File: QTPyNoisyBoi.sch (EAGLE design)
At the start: 32 parts, among them IC1 LD117AS50TR, IC2 TL074D, J1 WQP-PJ301M-12_JACK, J2 WQP-PJ301M-12_JACK, J3 WQP-PJ301M-12_JACK, J4 WQP-PJ301M-12_JACK, U1 ADAFRUIT_QTPYM0

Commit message: added cap on vmidref; various cleanup
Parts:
- added C9: (no value), rcl:C-EUC0603
- added R14: (no value), rcl:R-EU_R0603
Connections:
- new net N$5: J4.2, R14.2
- net GND: now also C9.1
- net RX: now also R14.1, U1.RX; no longer J4.2
- net VMIDREF: now also C9.2
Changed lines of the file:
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@@
 <part name="D2" library="SparkFun-DiscreteSemi" library_urn="urn:adsk.eagle:library:514" deviceset="DIODE-SCHOTTKY" device="-PMEG4005EJ" package3d_urn="urn:adsk.eagle:package:38441/1" value="0.5A/40V/420mV"/>
 <part name="D1" library="SparkFun-DiscreteSemi" library_urn="urn:adsk.eagle:library:514" deviceset="DIODE-SCHOTTKY" device="-PMEG4005EJ" package3d_urn="urn:adsk.eagle:package:38441/1" value="0.5A/40V/420mV"/>
+<part name="C9" library="rcl" library_urn="urn:adsk.eagle:library:334" deviceset="C-EU" device="C0603" package3d_urn="urn:adsk.eagle:package:23616/2"/>
+<part name="R14" library="rcl" library_urn="urn:adsk.eagle:library:334" deviceset="R-EU_" device="R0603" package3d_urn="urn:adsk.eagle:package:23555/3"/>
 </parts>
 <sheets>
@@
 <attribute name="VALUE" x="192.532" y="104.14" size="1.778" layer="96" font="vector" rot="R90" align="top-left"/>
 </instance>
+<instance part="C9" gate="G$1" x="63.5" y="5.08" smashed="yes" rot="R180">
+<attribute name="NAME" x="61.976" y="4.699" size="1.778" layer="95" rot="R180"/>
+<attribute name="VALUE" x="61.976" y="9.779" size="1.778" layer="96" rot="R180"/>
+</instance>
+<instance part="R14" gate="G$1" x="198.12" y="101.6" smashed="yes">
+<attribute name="NAME" x="194.31" y="103.0986" size="1.778" layer="95"/>
+<attribute name="VALUE" x="194.31" y="98.298" size="1.778" layer="96"/>
+</instance>
 </instances>
 <busses>
@@
 <pinref part="R11" gate="G$1" pin="1"/>
 <pinref part="GND14" gate="1" pin="GND"/>
+<pinref part="C9" gate="G$1" pin="1"/>
+<wire x1="63.5" y1="2.54" x2="71.12" y2="2.54" width="0.1524" layer="91"/>
+<junction x="71.12" y="2.54"/>
 </segment>
 <segment>
@@
 <junction x="71.12" y="12.7"/>
 <label x="76.2" y="12.7" size="1.778" layer="95"/>
+<wire x1="71.12" y1="12.7" x2="63.5" y2="12.7" width="0.1524" layer="91"/>
+<pinref part="C9" gate="G$1" pin="2"/>
+<wire x1="63.5" y1="12.7" x2="63.5" y2="10.16" width="0.1524" layer="91"/>
 </segment>
 <segment>
@@
 <net name="RX" class="0">
 <segment>
-<pinref part="J4" gate="G$1" pin="2"/>
-<wire x1="208.28" y1="101.6" x2="190.5" y2="101.6" width="0.1524" layer="91"/>
 <pinref part="D1" gate="G$1" pin="A"/>
+<pinref part="D2" gate="G$1" pin="C"/>
 <wire x1="190.5" y1="104.14" x2="190.5" y2="101.6" width="0.1524" layer="91"/>
-<pinref part="D2" gate="G$1" pin="C"/>
+<pinref part="R14" gate="G$1" pin="1"/>
 <wire x1="190.5" y1="101.6" x2="190.5" y2="99.06" width="0.1524" layer="91"/>
+<wire x1="193.04" y1="101.6" x2="190.5" y2="101.6" width="0.1524" layer="91"/>
 <junction x="190.5" y="101.6"/>
 <wire x1="190.5" y1="101.6" x2="175.26" y2="101.6" width="0.1524" layer="91"/>
 <label x="175.26" y="101.6" size="1.778" layer="95"/>
 </segment>
-</net>
+<segment>
+<pinref part="U1" gate="U$1" pin="RX"/>
+<wire x1="78.74" y1="45.72" x2="91.44" y2="45.72" width="0.1524" layer="91"/>
+<label x="83.82" y="45.72" size="1.778" layer="95"/>
+</segment>
+</net>
+<net name="N$5" class="0">
+<segment>
+<pinref part="R14" gate="G$1" pin="2"/>
+<pinref part="J4" gate="G$1" pin="2"/>
+<wire x1="203.2" y1="101.6" x2="208.28" y2="101.6" width="0.1524" layer="91"/>
+</segment>
+</net>

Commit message: sigh
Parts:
- added C10: 18pF, rcl:C-EUC0603
- added C11: (no value), rcl:C-EUC0603
- added D3, D4: 250mA/100V, halcyonmod_DiscreteSemi:DIODEBAS16
- added S1: MOMENTARY-SWITCH-SPST-PTH-6.0MM, SparkFun-Switches:MOMENTARY-SWITCH-SPST-PTH-6.0MM
- C4: value (none) -> 0.1uF
- R10, R11: value (none) -> 47k
- R4: value (none) -> 33k
- R5: value (none) -> 100k
- R6: value (none) -> 200
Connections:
- net N$2 renamed A1
- net N$3 renamed A2
- net N$4 renamed A3
- net VMIDREF renamed VBIAS
- removed net N$15: J2.2, R9.2
- new net N$12: D4.C, DIM1.-12V
- new net N$17: D3.A, DIM1.+12V
- new net N$18: C10.2, IC2A.OUT, R6.1
- new net N$2: S1.2, U1.TX
- new net N$8: IC2D.-IN, IC2D.OUT
- net +12V: now also D3.C; no longer DIM1.+12V
- net -12V: now also D4.A; no longer DIM1.-12V
- net GND: now also IC2D.+IN, S1.1
- net N$1: now also J2.2, R9.2; no longer IC2B.OUT, R9.1
- net N$10: now also C10.1
- net N$13: now also C11.1
- net N$14: now also C11.2, IC2B.OUT, R9.1; no longer J1.2, R6.2
- net N$9: now also J1.2, R6.2; no longer IC2A.OUT, R6.1
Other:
- moved on the sheet: C4, C5, C6, C7, D1, D2, J4, R14, R5, R6, R8, R9

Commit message: submit to fab
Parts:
- added C12: 18pF, rcl:C-EUC0603
- added R144: 220, rcl:R-EU_R0603
- C1, C2: value (none) -> 1uF
- C11: value (none) -> 18pF
- C3, C5, C6, C7, C8, C9: value (none) -> 0.1uF
- R1, R2, R3: value (none) -> 10k
- R10, R11: value 47k -> 33k
- R12, R7: value (none) -> 33k
- R13, R8: value (none) -> 100k
- R14, R9: value (none) -> 200
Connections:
- removed net N$16: J3.2, R13.2
- new net N$3: C12.2, IC2C.OUT, R14.1
- new net N$4: C12.1, C8.1, IC2C.+IN, R12.2, R13.1
- net A0: no longer C8.1, IC2C.+IN
- net N$11: now also J3.2, R13.2, R14.2; no longer IC2C.OUT, R12.2, R13.1
- net N$5: now also R144.2; no longer R14.2
- net RX: now also R144.1; no longer R14.1
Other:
- moved on the sheet: C1, C10, C11, C2, C3, C4, C5, C8, D1, D2, D3, D4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

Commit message: fix dumb +/- opamp input swap on B and C
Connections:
- net N$13: now also IC2B.-IN; no longer IC2B.+IN
- net N$4: now also IC2C.-IN; no longer IC2C.+IN
- net VBIAS: now also IC2B.+IN, IC2C.+IN; no longer IC2B.-IN, IC2C.-IN
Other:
- moved on the sheet: IC2B, IC2C
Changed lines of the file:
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@@
 <part name="C12" library="rcl" library_urn="urn:adsk.eagle:library:334" deviceset="C-EU" device="C0603" package3d_urn="urn:adsk.eagle:package:23616/2" value="18pF"/>
 <part name="R12" library="rcl" library_urn="urn:adsk.eagle:library:334" deviceset="R-EU_" device="R0603" package3d_urn="urn:adsk.eagle:package:23555/3" value="33k"/>
-<part name="FRAME1" library="frames" library_urn="urn:adsk.eagle:library:229" deviceset="A3L-LOC" device=""/>
+<part name="FRAME1" library="frames" library_urn="urn:adsk.eagle:library:229" deviceset="A3L-LOC" device="" value="QTPyNoisyBoi"/>
 </parts>
 <sheets>
@@
 <attribute name="VALUE" x="139.7" y="71.12" size="1.778" layer="96" rot="MR180"/>
 </instance>
-<instance part="IC2" gate="B" x="139.7" y="20.32" smashed="yes">
-<attribute name="NAME" x="142.24" y="23.495" size="1.778" layer="95"/>
-<attribute name="VALUE" x="141.224" y="14.732" size="1.778" layer="96"/>
-</instance>
-<instance part="IC2" gate="C" x="139.7" y="-27.94" smashed="yes">
-<attribute name="NAME" x="142.24" y="-24.765" size="1.778" layer="95"/>
-<attribute name="VALUE" x="142.24" y="-33.02" size="1.778" layer="96"/>
+<instance part="IC2" gate="B" x="139.7" y="20.32" smashed="yes" rot="MR180">
+<attribute name="NAME" x="142.24" y="17.145" size="1.778" layer="95" rot="MR180"/>
+<attribute name="VALUE" x="141.224" y="25.908" size="1.778" layer="96" rot="MR180"/>
+</instance>
+<instance part="IC2" gate="C" x="139.7" y="-27.94" smashed="yes" rot="MR180">
+<attribute name="NAME" x="142.24" y="-31.115" size="1.778" layer="95" rot="MR180"/>
+<attribute name="VALUE" x="142.24" y="-22.86" size="1.778" layer="96" rot="MR180"/>
 </instance>
 <instance part="IC2" gate="D" x="139.7" y="-60.96" smashed="yes">
@@
 <pinref part="R7" gate="G$1" pin="2"/>
 <wire x1="127" y1="22.86" x2="129.54" y2="22.86" width="0.1524" layer="91"/>
-<pinref part="IC2" gate="B" pin="+IN"/>
-<wire x1="132.08" y1="22.86" x2="129.54" y2="22.86" width="0.1524" layer="91"/>
-<junction x="129.54" y="22.86"/>
 <pinref part="C11" gate="G$1" pin="1"/>
 <wire x1="129.54" y1="33.02" x2="134.62" y2="33.02" width="0.1524" layer="91"/>
 <junction x="129.54" y="33.02"/>
+<pinref part="IC2" gate="B" pin="-IN"/>
+<wire x1="129.54" y1="22.86" x2="132.08" y2="22.86" width="0.1524" layer="91"/>
+<junction x="129.54" y="22.86"/>
 </segment>
 </net>
@@
 </segment>
 <segment>
-<pinref part="IC2" gate="B" pin="-IN"/>
+<pinref part="IC2" gate="B" pin="+IN"/>
 <wire x1="132.08" y1="17.78" x2="119.38" y2="17.78" width="0.1524" layer="91"/>
 <label x="119.38" y="17.78" size="1.778" layer="95"/>
 </segment>
 <segment>
-<pinref part="IC2" gate="C" pin="-IN"/>
+<pinref part="IC2" gate="C" pin="+IN"/>
 <wire x1="132.08" y1="-30.48" x2="119.38" y2="-30.48" width="0.1524" layer="91"/>
-<label x="119.38" y="-30.48" size="1.778" layer="95"/>
 </segment>
 </net>
@@
 <net name="N$4" class="0">
 <segment>
-<pinref part="IC2" gate="C" pin="+IN"/>
 <pinref part="R12" gate="G$1" pin="2"/>
-<wire x1="132.08" y1="-25.4" x2="129.54" y2="-25.4" width="0.1524" layer="91"/>
 <pinref part="C12" gate="G$1" pin="1"/>
 <wire x1="129.54" y1="-25.4" x2="127" y2="-25.4" width="0.1524" layer="91"/>
 <wire x1="134.62" y1="-17.78" x2="129.54" y2="-17.78" width="0.1524" layer="91"/>
 <wire x1="129.54" y1="-17.78" x2="129.54" y2="-25.4" width="0.1524" layer="91"/>
-<junction x="129.54" y="-25.4"/>
 <pinref part="R13" gate="G$1" pin="1"/>
 <wire x1="134.62" y1="-10.16" x2="129.54" y2="-10.16" width="0.1524" layer="91"/>
@@
 <wire x1="129.54" y1="-2.54" x2="129.54" y2="-10.16" width="0.1524" layer="91"/>
 <junction x="129.54" y="-10.16"/>
+<pinref part="IC2" gate="C" pin="-IN"/>
+<wire x1="129.54" y1="-25.4" x2="132.08" y2="-25.4" width="0.1524" layer="91"/>
+<junction x="129.54" y="-25.4"/>
 </segment>
 </net>
@@
 </sheet>
 </sheets>
+<errors>
+</errors>
 </schematic>
 </drawing>

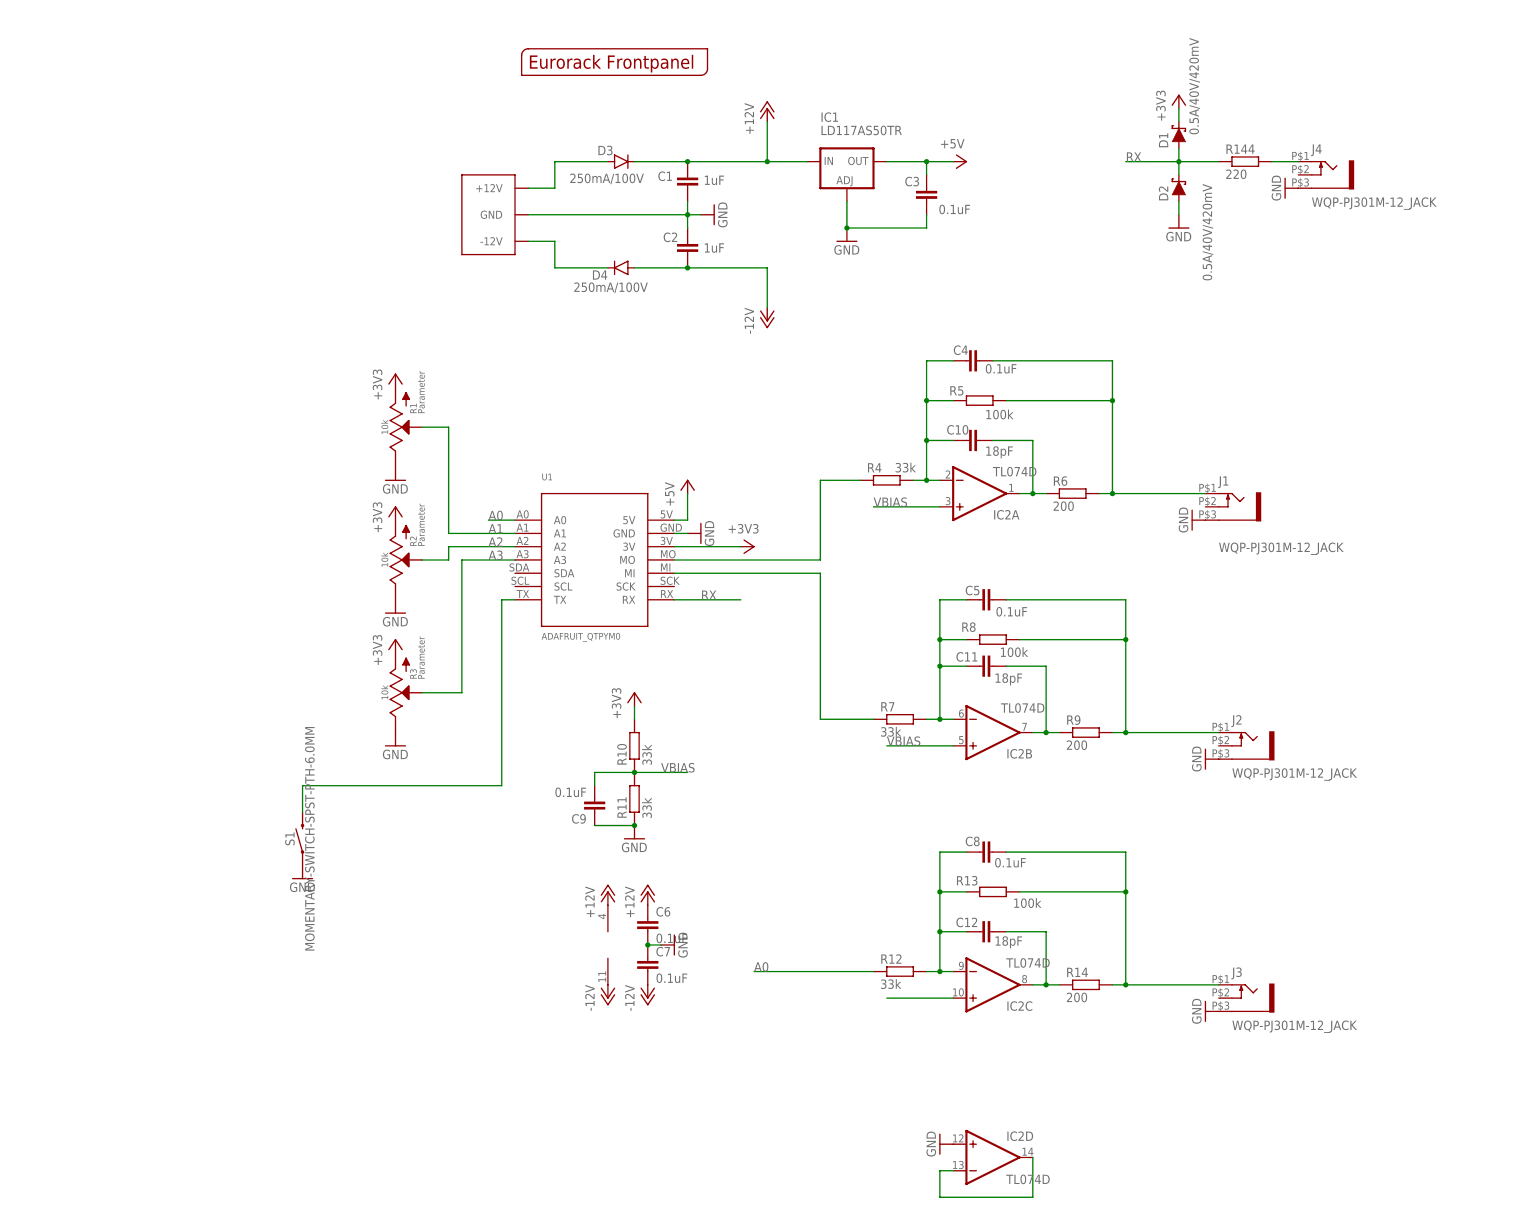
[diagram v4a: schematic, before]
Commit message: added 2nd button
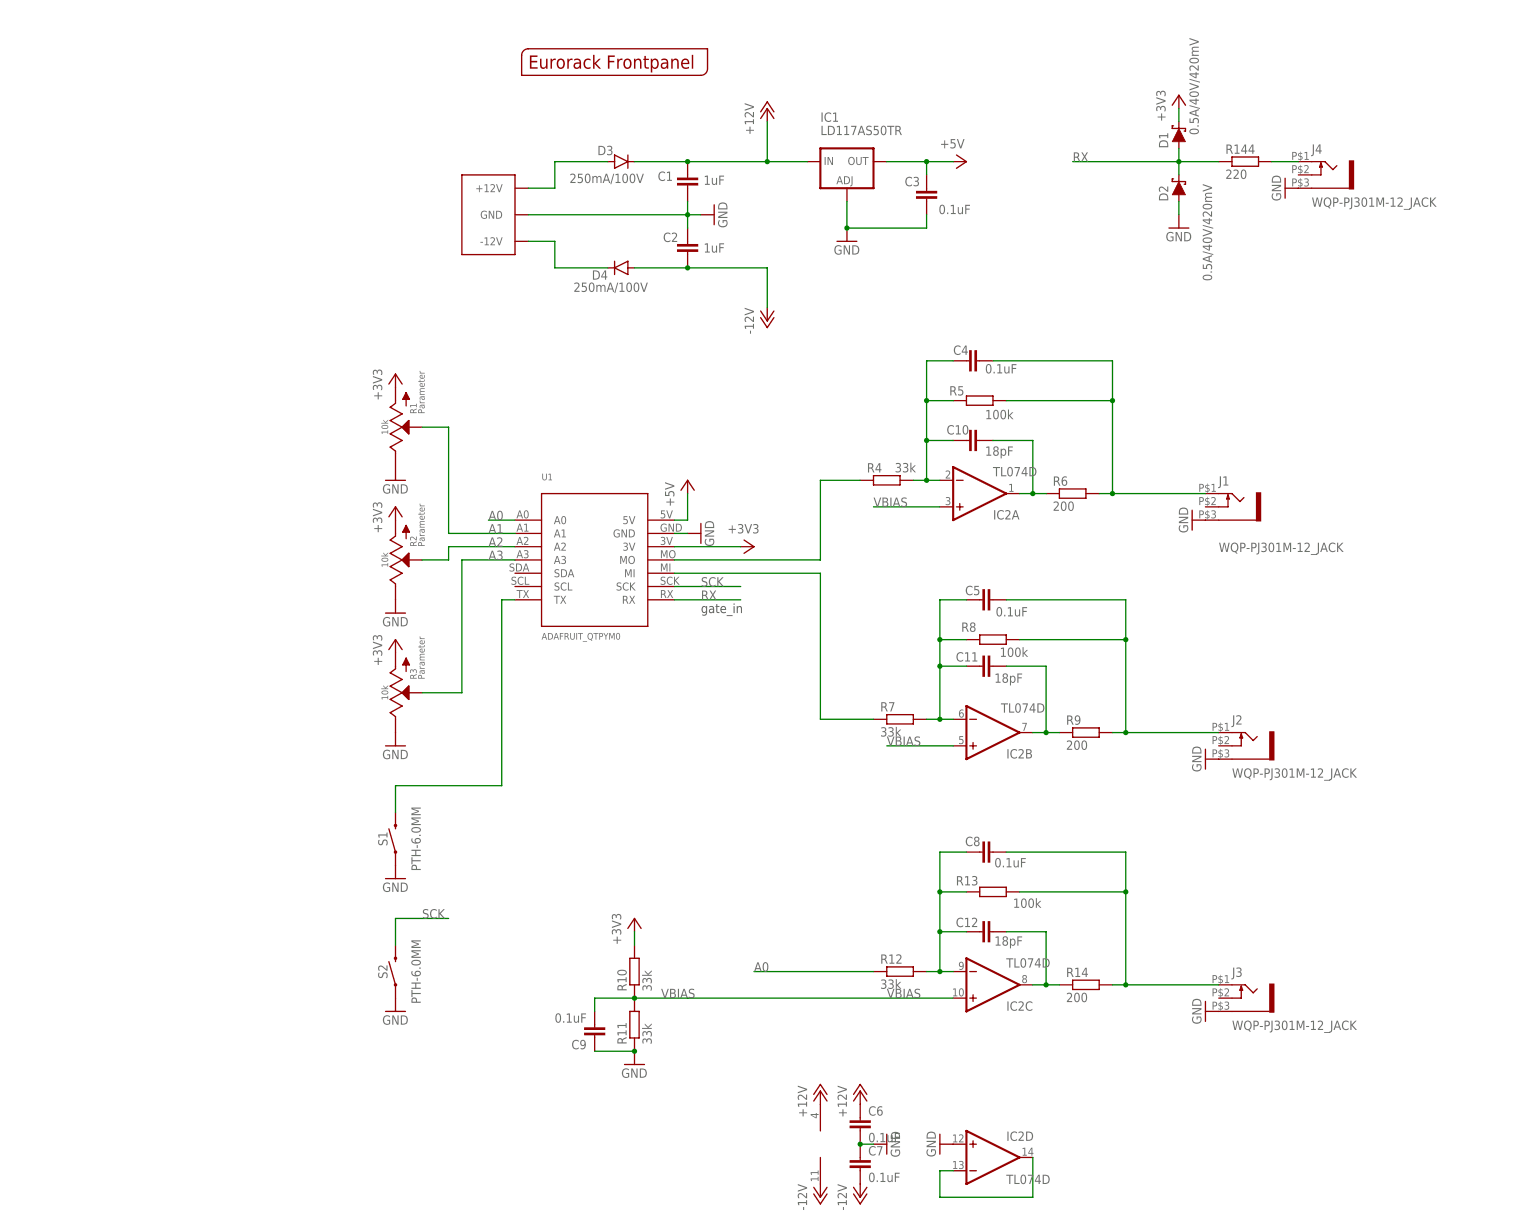
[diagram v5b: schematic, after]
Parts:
- added S2: PTH-6.0MM, SparkFun-Switches:MOMENTARY-SWITCH-SPST-PTH-6.0MM
- C1, C10, C11, C12, C2, C3, C4, C5, C6, C7, C8, C9: device rcl:C-EUC0603 -> rcl:C-EUC0805
- R10, R11, R12, R13, R14, R144, R4, R5, R6, R7, R8, R9: device rcl:R-EU_R0603 -> rcl:R-EU_R0805
- S1: value MOMENTARY-SWITCH-SPST-PTH-6.0MM -> PTH-6.0MM
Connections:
- new net SCK: S2.2, U1.SCK
- net GND: now also S2.1
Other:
- note added: "gate_in"
- moved on the sheet: C6, C7, C9, R10, R11, S1

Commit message: added neopixels, woorah
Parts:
- added LED1, LED2, LED3: WS2812B5050, todstuff:WS2812B5050
- C4, C5, C8: value 0.1uF -> 10nF
- R15: value 220 -> 200
- renumbered R144 to R15
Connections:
- new net N$15: LED1.DO, LED2.DI
- new net N$16: LED2.DO, LED3.DI
- new net SDA: LED1.DI, U1.SDA
- net +3V3: now also LED1.VDD, LED2.VDD, LED3.VDD
- net GND: now also LED1.GND, LED2.GND, LED3.GND
